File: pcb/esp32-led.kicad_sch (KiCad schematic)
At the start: 0 parts

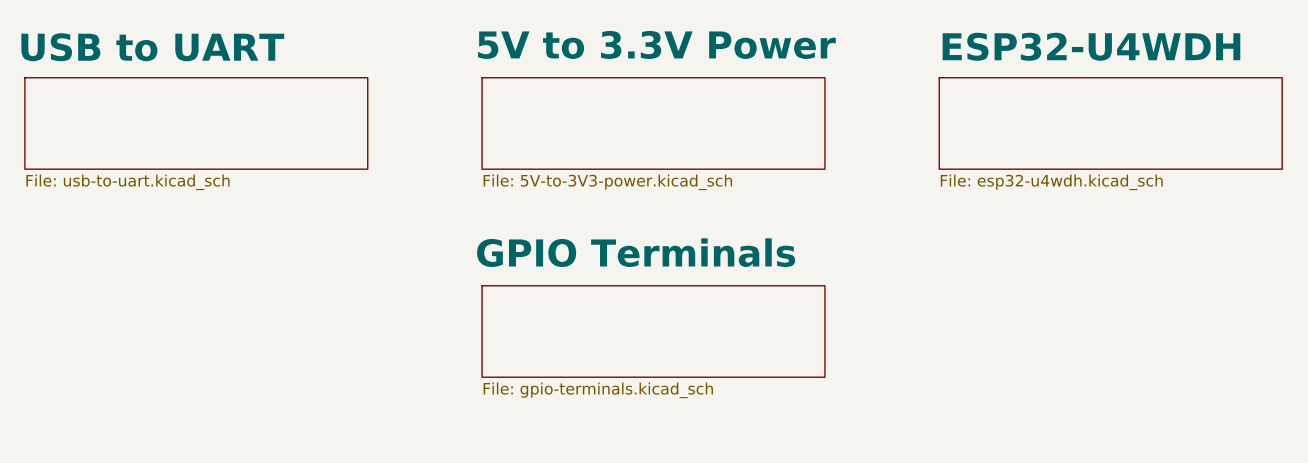
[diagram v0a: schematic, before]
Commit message: ADD subfolder for pcb
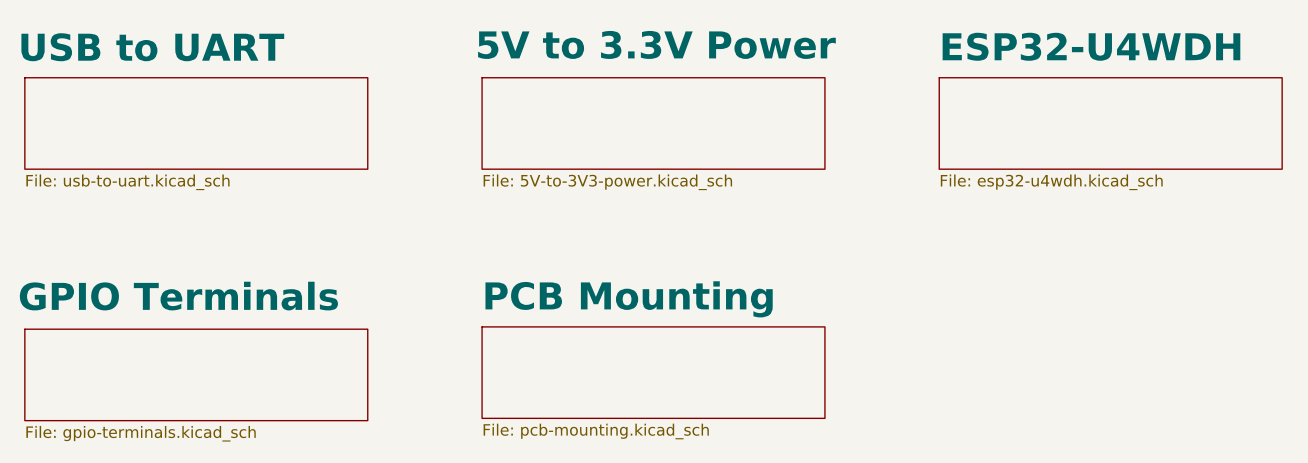
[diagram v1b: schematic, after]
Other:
- added sheet PCB Mounting (pcb-mounting.kicad_sch)
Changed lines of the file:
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@@
     )
   )
-  (sheet (at 127 112.014) (size 38.1 10.16)
+  (sheet (at 76.2 116.84) (size 38.1 10.16)
     (stroke (width 0.1524) (type solid) (color 161 110 18 1))
     (fill (color 161 110 18 1.0000))
-    (property "Sheet name" "GPIO Terminals" (id 0) (at 126.238 110.236 0)
+    (property "Sheet name" "GPIO Terminals" (id 0) (at 75.438 115.062 0)
       (effects (font (size 3 3) bold) (justify left bottom))
     )
-    (property "Sheet file" "gpio-terminals.kicad_sch" (id 1) (at 127 122.7586 0)
+    (property "Sheet file" "gpio-terminals.kicad_sch" (id 1) (at 76.2 127.5846 0)
       (effects (font (size 1.27 1.27)) (justify left top))
     )
@@
     )
   )
+  (sheet (at 127 116.586) (size 38.1 10.16) (fields_autoplaced)
+    (stroke (width 0.1524) (type solid) (color 255 117 69 1))
+    (fill (color 255 117 69 1.0000))
+    (property "Sheet name" "PCB Mounting" (id 0) (at 127 115.0094 0)
+      (effects (font (size 3 3) bold) (justify left bottom))
+    )
+    (property "Sheet file" "pcb-mounting.kicad_sch" (id 1) (at 127 127.3306 0)
+      (effects (font (size 1.27 1.27)) (justify left top))
+    )
+  )
   (sheet_instances
     (path "/" (page "1"))
@@
     (path "/82d2196d-ce03-415b-a1fb-abc76be70a22" (page "3"))
     (path "/87ef5048-9cc7-4da1-8293-682ac74ffe8b" (page "4"))
+    (path "/c2f88748-7e50-45f6-b4e9-430e89c3a365" (page "6"))
   )
   (symbol_instances
@@
       (reference "D3") (unit 1) (value "LED") (footprint "LED_SMD:LED_0402_1005Metric")
     )
+    (path "/c2f88748-7e50-45f6-b4e9-430e89c3a365/d821a4f9-c362-4a56-93a0-45312ac35c4f"
+      (reference "H1") (unit 1) (value "MountingHole") (footprint "MountingHole:MountingHole_3.2mm_M3_DIN965")
+    )
+    (path "/c2f88748-7e50-45f6-b4e9-430e89c3a365/8d063cbe-42d4-4d93-93cd-49d4b790f576"
+      (reference "H2") (unit 1) (value "MountingHole") (footprint "MountingHole:MountingHole_3.2mm_M3_DIN965")
+    )
     (path "/87ef5048-9cc7-4da1-8293-682ac74ffe8b/383e7bdd-113d-444e-b407-58233881efeb"
